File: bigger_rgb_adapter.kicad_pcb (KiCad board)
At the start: 2 copper layers, 11.4 x 26.7 mm, 7 parts, among them J1 Conn_01x10, J2 Conn_01x10

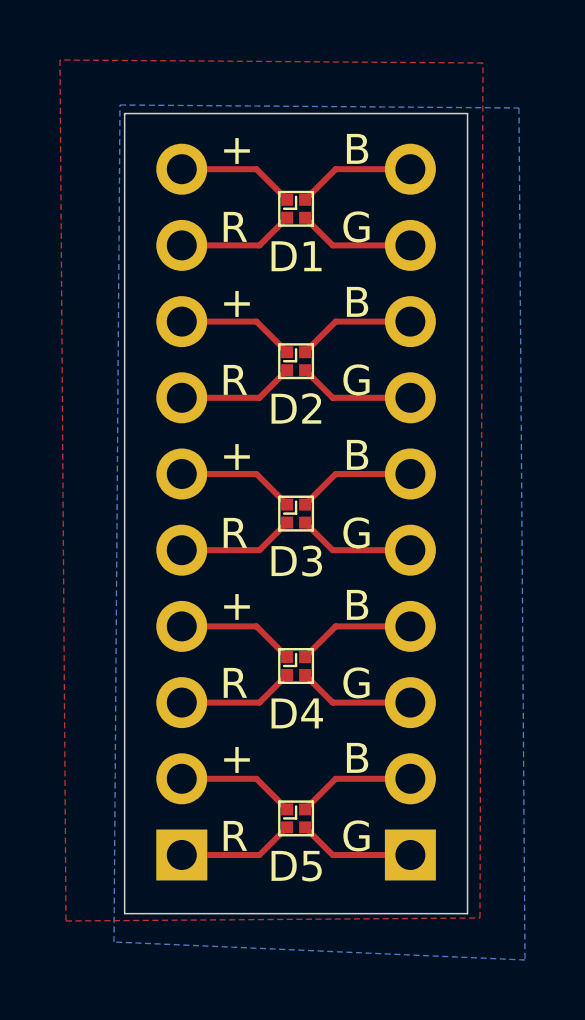
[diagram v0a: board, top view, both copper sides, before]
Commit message: Use EAST1616RGBA3 LEDs instead
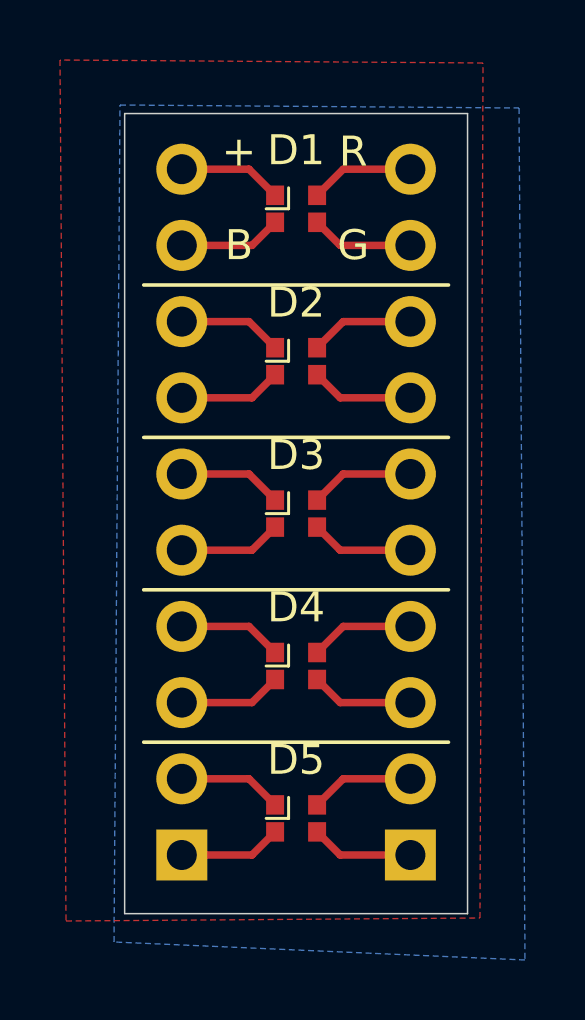
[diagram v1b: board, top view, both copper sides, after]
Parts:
- D1, D2, D3, D4, D5: footprint LED_SMD:LED_Cree-UHD1110-FKA_1x1mm -> LED_SMD:LED_RGB_EAST1616RGBA3
- turned D1 to 180 degrees
- turned D2 to 180 degrees
- turned D3 to 180 degrees
- turned D4 to 180 degrees
- turned D5 to 180 degrees
